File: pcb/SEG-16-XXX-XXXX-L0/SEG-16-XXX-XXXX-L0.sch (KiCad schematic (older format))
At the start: 191 parts, among them J1 0472861001, J2 0472861001, J3 DTA_FLOW_LEFT, J4 DATA_FLOW_RIGHT, U1 STM8S003, U2 TM1640

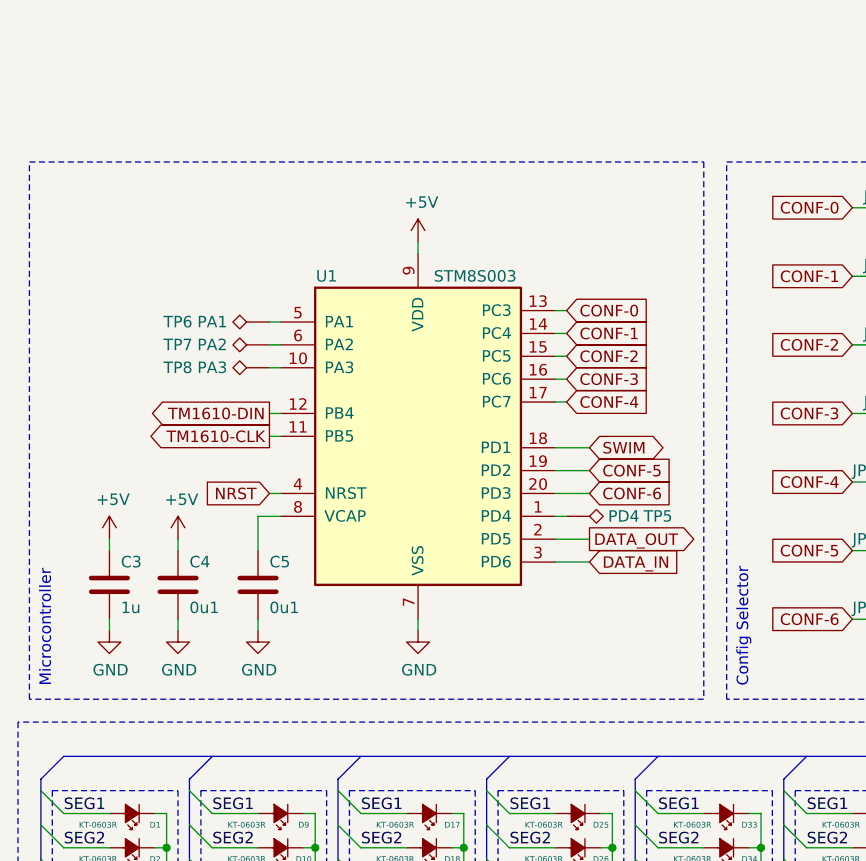
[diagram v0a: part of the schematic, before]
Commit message: Updated to 0V6 changed images
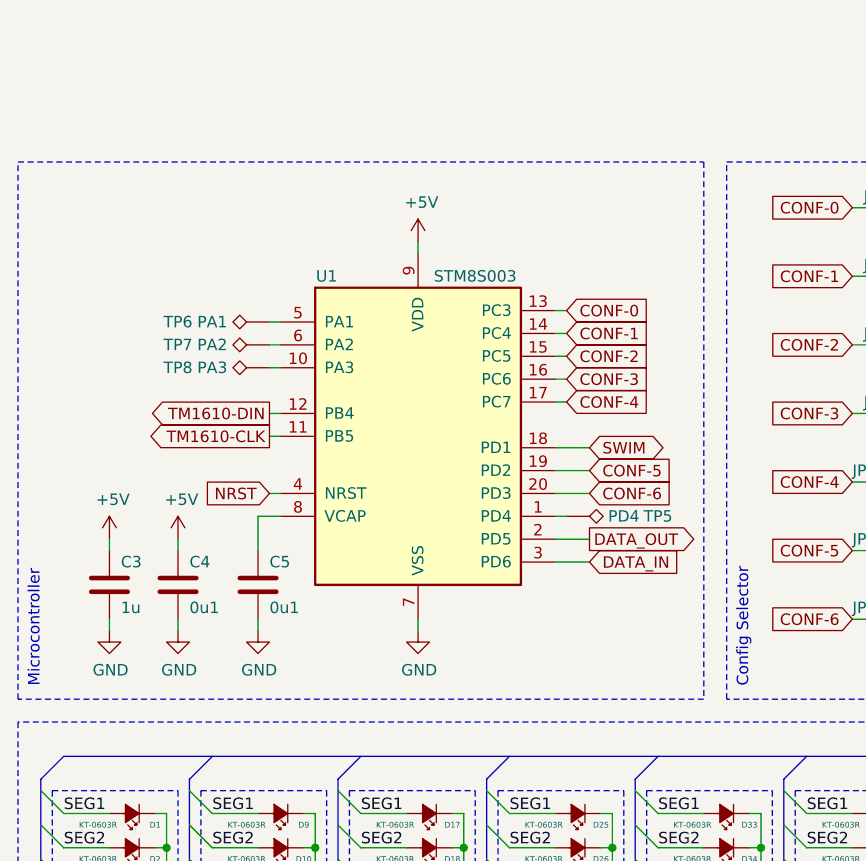
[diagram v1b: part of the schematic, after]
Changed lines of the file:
@@
 Wire Wire Line
 	1650 4250 1750 4250
-Text Notes 750  5000 1    50   ~ 0
+Text Notes 700  5000 1    50   ~ 0
 Microcontroller
 Wire Notes Line
-	3600 5050 650  5050
+	3600 5050 600  5050
 Wire Notes Line
-	650  5050 650  2700
+	600  5050 600  2700
 Wire Notes Line
-	650  2700 3600 2700
+	600  2700 3600 2700
 Wire Notes Line
 	3600 2700 3600 5050
